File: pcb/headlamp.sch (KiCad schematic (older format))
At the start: 57 parts, among them IC1 ATTINY841-SSU, P1 POWER, P2 SERIAL, P3 ISP, Q1 NX2301P, Q2 VEMT3700-GS08, Q3 DMP2035U, Q4 DMP2035U, SW1 BT2, SW2 BT1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

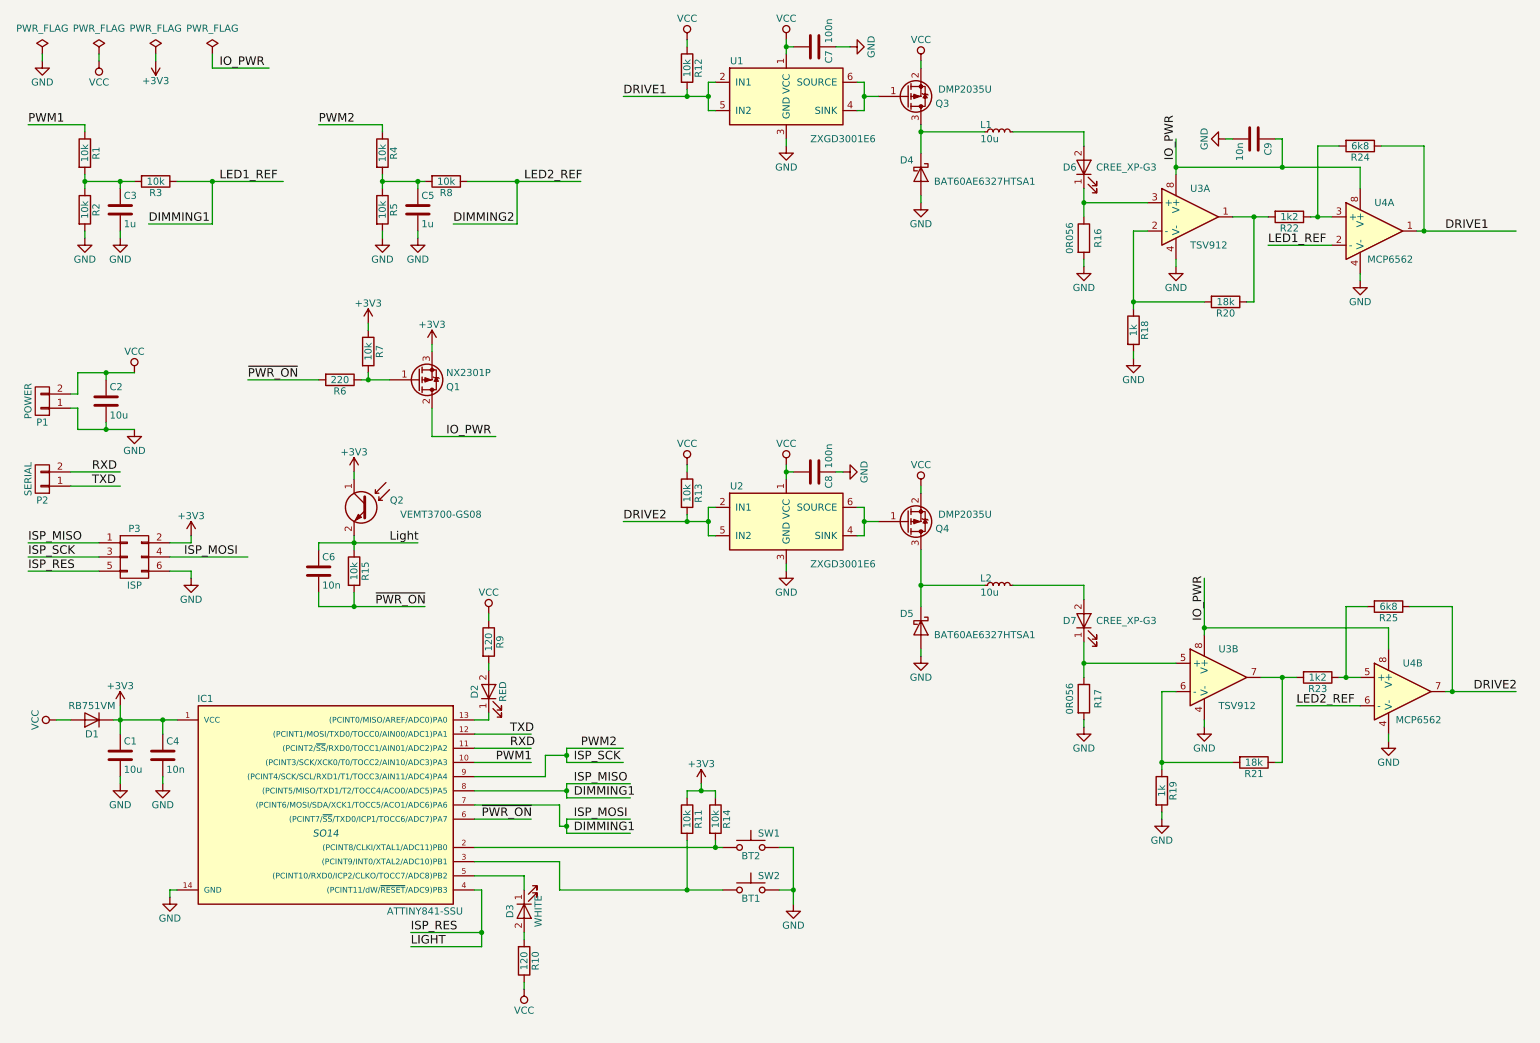
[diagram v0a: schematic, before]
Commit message: Switched to open drain comparator
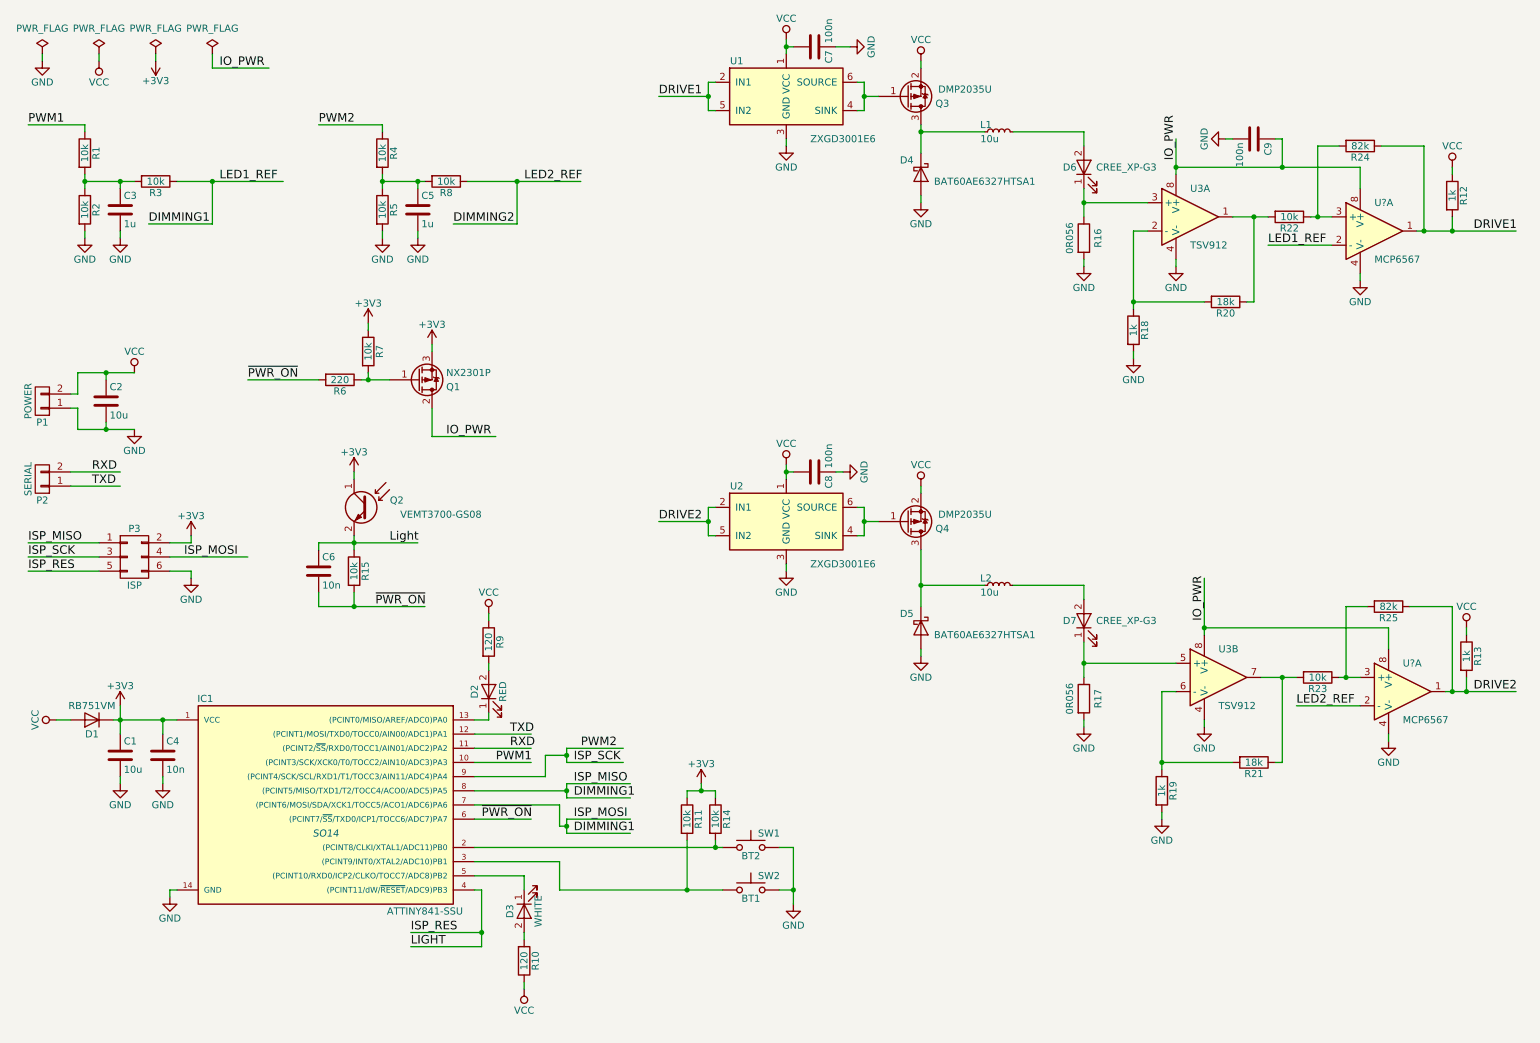
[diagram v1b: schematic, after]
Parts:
- removed U4: MCP6562, Housings_SOIC:SOIC-8-1EP_3.9x4.9mm_Pitch1.27mm, symbol MCP6562
- added U? (x2): MCP6567, symbol MCP6567
- C9: value 10n -> 100n
- R12, R13: value 10k -> 1k
- R22, R23: value 1k2 -> 10k
- R24, R25: value 6k8 -> 82k
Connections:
- wire segments 197 -> 243
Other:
- moved on the sheet: R12, R13

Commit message: Board added
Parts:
- removed C2: 10u, symbol C
- removed P2: SERIAL, symbol CONN_01X02
- removed Q1: NX2301P, symbol Q_PMOS_GDS
- added C10: 100n, Capacitors_SMD:C_0603, symbol C
- added P2: SERIAL, Connectors:GS3, symbol CONN_01X03
- added Q2: NX2301P, TO_SOT_Packages_SMD:SOT-23, symbol Q_PMOS_GSD
- C1, C7, C8, C9: footprint (none) -> Capacitors_SMD:C_0603
- C2: renamed from C3; footprint (none) -> Capacitors_SMD:C_0603
- C4: value 10n -> 100n; footprint (none) -> Capacitors_SMD:C_0603
- C5: renamed from C6; footprint (none) -> Capacitors_SMD:C_0603
- C6: renamed from C5; footprint (none) -> Capacitors_SMD:C_0603
- D1, D4, D5: footprint (none) -> Diodes_SMD:SOD-323
- D2, D3: footprint (none) -> LEDs:LED_PLCC-2
- D6, D7, P1: footprint (none) -> custom:Custom_Conn_2_Big
- IC1: footprint SO14 -> Housings_SOIC:SOIC-14_3.9x8.7mm_Pitch1.27mm
- L1, L2: footprint (none) -> Inductors:Inductor_Bourns-SRU8043
- P3: footprint (none) -> TO_SOT_Packages_SMD:SOT-23-6
- Q1: renamed from Q2; footprint (none) -> LEDs:LED_PLCC-2
- Q3, Q4: footprint (none) -> TO_SOT_Packages_SMD:SOT-23
- R1, R2, R3: footprint (none) -> Resistors_SMD:R_0603
- R10: renamed from R9; footprint (none) -> Resistors_SMD:R_0603
- R11: renamed from R10; footprint (none) -> Resistors_SMD:R_0603
- R12: renamed from R11; footprint (none) -> Resistors_SMD:R_0603
- R13: renamed from R14; footprint (none) -> Resistors_SMD:R_0603
- R14: renamed from R16; footprint (none) -> Resistors_SMD:R_1206
- R15: renamed from R17; footprint (none) -> Resistors_SMD:R_1206
- R16: renamed from R18; footprint (none) -> Resistors_SMD:R_0603
- R17: renamed from R19; footprint (none) -> Resistors_SMD:R_0603
- R18: renamed from R20; footprint (none) -> Resistors_SMD:R_0603
- R19: renamed from R21; footprint (none) -> Resistors_SMD:R_0603
- R20: renamed from R22; footprint (none) -> Resistors_SMD:R_0603
- R21: renamed from R23; footprint (none) -> Resistors_SMD:R_0603
- R22: renamed from R24; footprint (none) -> Resistors_SMD:R_0603
- R23: renamed from R25; footprint (none) -> Resistors_SMD:R_0603
- R24: renamed from R12; footprint (none) -> Resistors_SMD:R_0603
- R25: renamed from R13; footprint (none) -> Resistors_SMD:R_0603
- R4: renamed from R6; footprint (none) -> Resistors_SMD:R_0603
- R5: renamed from R15; footprint (none) -> Resistors_SMD:R_0603
- R6: renamed from R7; footprint (none) -> Resistors_SMD:R_0603
- R7: renamed from R4; footprint (none) -> Resistors_SMD:R_0603
- R8: renamed from R5; footprint (none) -> Resistors_SMD:R_0603
- R9: renamed from R8; footprint (none) -> Resistors_SMD:R_0603
- SW1, SW2: footprint (none) -> Buttons_Switches_SMD:SW_SPST_FSMSM
- U3: footprint Housings_SSOP:MSOP-8-1EP_3x3mm_Pitch0.65mm -> Housings_SSOP:MSOP-8_3x3mm_Pitch0.65mm
- U4: renamed from U?; footprint (none) -> Housings_SSOP:MSOP-8_3x3mm_Pitch0.65mm
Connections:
- wire segments 243 -> 202
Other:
- moved on the sheet: D3, P1, R11, SW1, SW2

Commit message: Final schematic values, pcb
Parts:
- C7, C8: value 100n -> 1u
- R10, R11: value 120 -> 220
- R20, R21: value 10k -> 12k
- R22, R23: value 82k -> 270k
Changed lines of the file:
@@
 P 10050 1450
 F 0 "R22" V 10130 1450 50  0000 C CNN
-F 1 "82k" V 10050 1450 50  0000 C CNN
+F 1 "270k" V 10050 1450 50  0000 C CNN
 F 2 "Resistors_SMD:R_0603" V 9980 1450 50  0001 C CNN
 F 3 "" H 10050 1450 50  0000 C CNN
@@
 P 9550 1950
 F 0 "R20" V 9630 1950 50  0000 C CNN
-F 1 "10k" V 9550 1950 50  0000 C CNN
+F 1 "12k" V 9550 1950 50  0000 C CNN
 F 2 "Resistors_SMD:R_0603" V 9480 1950 50  0001 C CNN
 F 3 "" H 9550 1950 50  0000 C CNN
@@
 P 4300 7300
 F 0 "R11" V 4380 7300 50  0000 C CNN
-F 1 "120" V 4300 7300 50  0000 C CNN
+F 1 "220" V 4300 7300 50  0000 C CNN
 F 2 "Resistors_SMD:R_0603" V 4230 7300 50  0001 C CNN
 F 3 "" H 4300 7300 50  0000 C CNN
@@
 P 10250 4700
 F 0 "R23" V 10330 4700 50  0000 C CNN
-F 1 "82k" V 10250 4700 50  0000 C CNN
+F 1 "270k" V 10250 4700 50  0000 C CNN
 F 2 "Resistors_SMD:R_0603" V 10180 4700 50  0001 C CNN
 F 3 "" H 10250 4700 50  0000 C CNN
@@
 P 9750 5200
 F 0 "R21" V 9830 5200 50  0000 C CNN
-F 1 "10k" V 9750 5200 50  0000 C CNN
+F 1 "12k" V 9750 5200 50  0000 C CNN
 F 2 "Resistors_SMD:R_0603" V 9680 5200 50  0001 C CNN
 F 3 "" H 9750 5200 50  0000 C CNN
@@
 P 3900 4950
 F 0 "R10" V 3980 4950 50  0000 C CNN
-F 1 "120" V 3900 4950 50  0000 C CNN
+F 1 "220" V 3900 4950 50  0000 C CNN
 F 2 "Resistors_SMD:R_0603" V 3830 4950 50  0001 C CNN
 F 3 "" H 3900 4950 50  0000 C CNN
@@
 P 6200 3750
 F 0 "C8" H 6225 3850 50  0000 L CNN
-F 1 "100n" H 6000 3850 50  0000 L CNN
+F 1 "1u" H 6000 3850 50  0000 L CNN
 F 2 "Capacitors_SMD:C_0603" H 6238 3600 50  0001 C CNN
 F 3 "" H 6200 3750 50  0000 C CNN
@@
 P 6200 750
 F 0 "C7" H 6225 850 50  0000 L CNN
-F 1 "100n" H 6000 850 50  0000 L CNN
+F 1 "1u" H 6000 850 50  0000 L CNN
 F 2 "Capacitors_SMD:C_0603" H 6238 600 50  0001 C CNN
 F 3 "" H 6200 750 50  0000 C CNN

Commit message: Updated capacitors values
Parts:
- C10, C9: value 100n -> 10n
- C4: value 100n -> 1u
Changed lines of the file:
@@
 P 1600 5750
 F 0 "C4" H 1625 5850 50  0000 L CNN
-F 1 "100n" H 1625 5650 50  0000 L CNN
+F 1 "1u" H 1625 5650 50  0000 L CNN
 F 2 "Capacitors_SMD:C_0603" H 1638 5600 50  0001 C CNN
 F 3 "" H 1600 5750 50  0000 C CNN
@@
 P 9300 1400
 F 0 "C9" H 9325 1500 50  0000 L CNN
-F 1 "100n" H 9325 1300 50  0000 L CNN
+F 1 "10n" H 9325 1300 50  0000 L CNN
 F 2 "Capacitors_SMD:C_0603" H 9338 1250 50  0001 C CNN
 F 3 "" H 9300 1400 50  0000 C CNN
@@
 P 9500 4600
 F 0 "C10" H 9525 4700 50  0000 L CNN
-F 1 "100n" H 9525 4500 50  0000 L CNN
+F 1 "10n" H 9525 4500 50  0000 L CNN
 F 2 "Capacitors_SMD:C_0603" H 9538 4450 50  0001 C CNN
 F 3 "" H 9500 4600 50  0000 C CNN

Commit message: Replaced diode by resistor - was causing rising mcu VCC from spikes on power lines
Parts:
- removed D1: RB751VM, Diodes_SMD:SOD-323, symbol D
- added R26: 33, Resistors_SMD:R_0603, symbol R
- D6, D7: value CREE_XP-G3 -> LED
- R1, R7: value 10k -> 8k2
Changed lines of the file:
@@
 P 8100 1600
 F 0 "D6" V 8100 1700 50  0000 C CNN
-F 1 "CREE_XP-G3" V 8100 1300 50  0000 C CNN
+F 1 "LED" V 8100 1450 50  0000 C CNN
 F 2 "custom:Custom_Conn_2_Big" H 8100 1600 50  0001 C CNN
 F 3 "" H 8100 1600 50  0000 C CNN
@@
 P 3150 1500
 F 0 "R7" V 3230 1500 50  0000 C CNN
-F 1 "10k" V 3150 1500 50  0000 C CNN
+F 1 "8k2" V 3150 1500 50  0000 C CNN
 F 2 "Resistors_SMD:R_0603" V 3080 1500 50  0001 C CNN
 F 3 "" H 3150 1500 50  0000 C CNN
@@
 P 1050 1500
 F 0 "R1" V 1130 1500 50  0000 C CNN
-F 1 "10k" V 1050 1500 50  0000 C CNN
+F 1 "8k2" V 1050 1500 50  0000 C CNN
 F 2 "Resistors_SMD:R_0603" V 980 1500 50  0001 C CNN
 F 3 "" H 1050 1500 50  0000 C CNN
@@
 $EndComp
 $Comp
-L D D1
-U 1 1 58323970
-P 1100 5500
-F 0 "D1" H 1100 5600 50  0000 C CNN
-F 1 "RB751VM" H 1100 5400 50  0000 C CNN
-F 2 "Diodes_SMD:SOD-323" H 1100 5500 50  0001 C CNN
-F 3 "" H 1100 5500 50  0000 C CNN
-	1    1100 5500
-	-1   0    0    1
-$EndComp
-$Comp
 L VCC #PWR015
 U 1 1 58323BD9
@@
 P 8100 4800
 F 0 "D7" V 8100 4900 50  0000 C CNN
-F 1 "CREE_XP-G3" V 8100 4500 50  0000 C CNN
+F 1 "LED" V 8100 4650 50  0000 C CNN
 F 2 "custom:Custom_Conn_2_Big" H 8100 4800 50  0001 C CNN
 F 3 "" H 8100 4800 50  0000 C CNN
@@
 	1150 3350 1150 3400
 Connection ~ 1150 3400
+$Comp
+L R R26
+U 1 1 58FCEB2F
+P 1100 5500
+F 0 "R26" V 1180 5500 50  0000 C CNN
+F 1 "33" V 1100 5500 50  0000 C CNN
+F 2 "Resistors_SMD:R_0603" V 1030 5500 50  0001 C CNN
+F 3 "" H 1100 5500 50  0001 C CNN
+	1    1100 5500
+	0    1    1    0
+$EndComp
 $EndSCHEMATC
